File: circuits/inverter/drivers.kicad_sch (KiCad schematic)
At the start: 2 parts

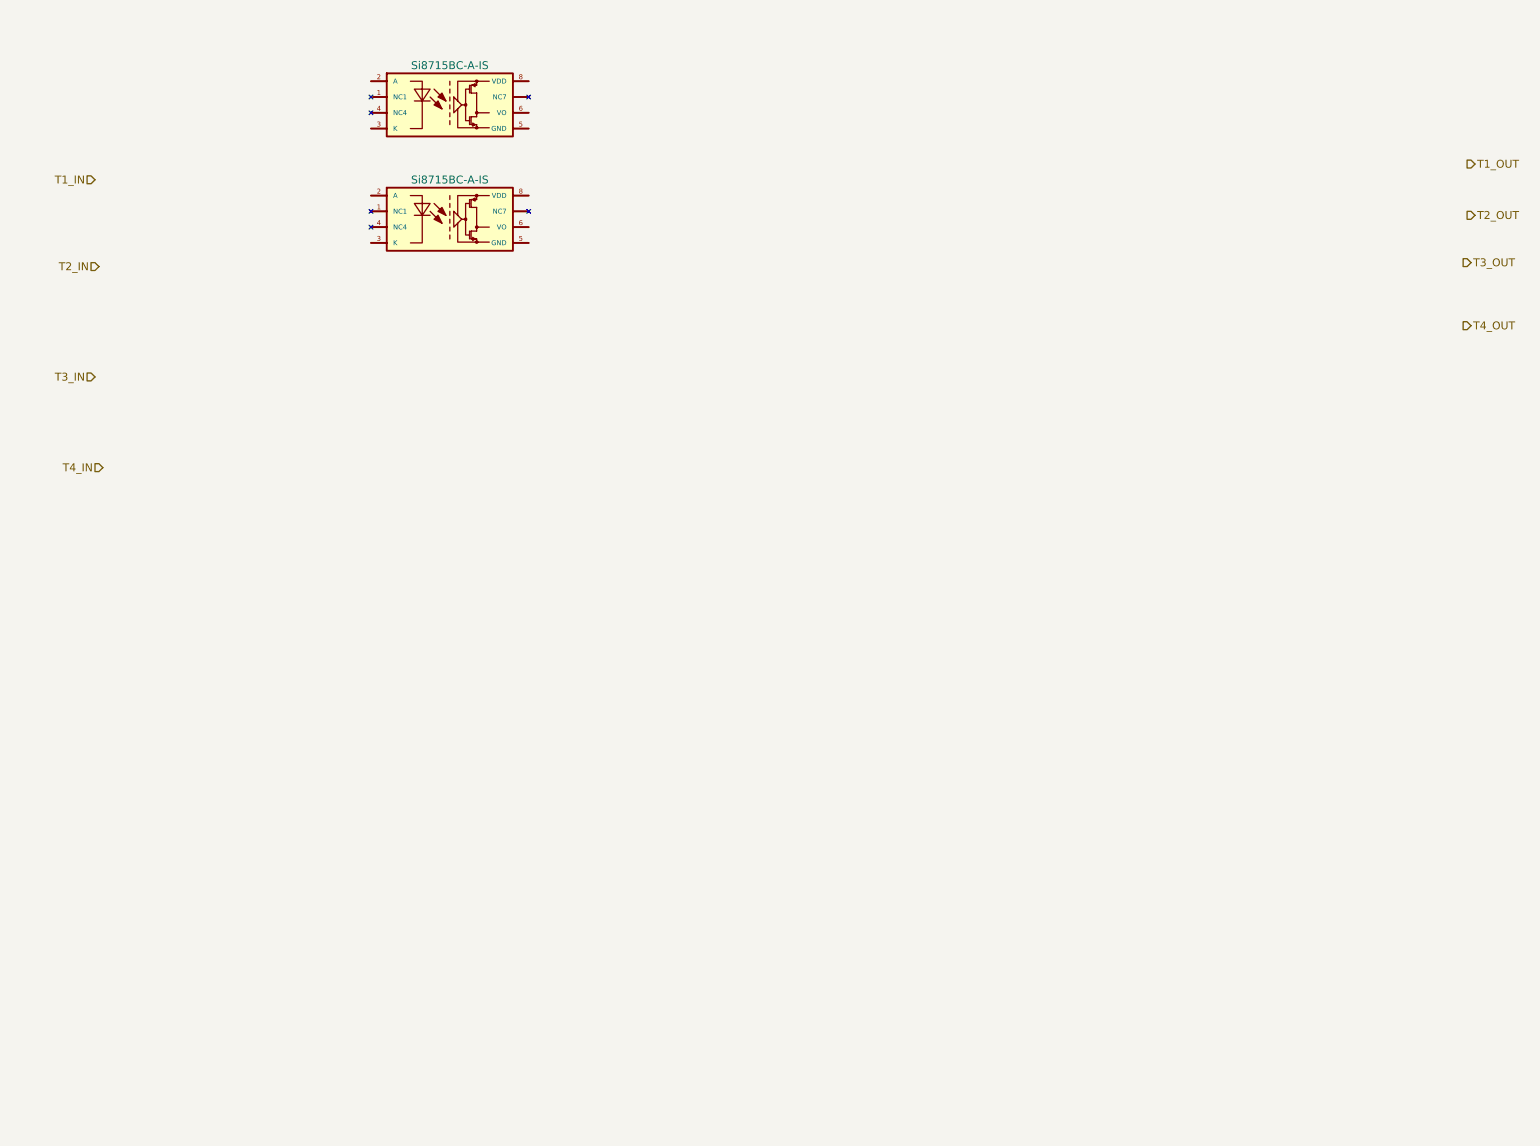
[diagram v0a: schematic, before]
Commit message: converts libraries to Kicad 6 format, updates bridge driver
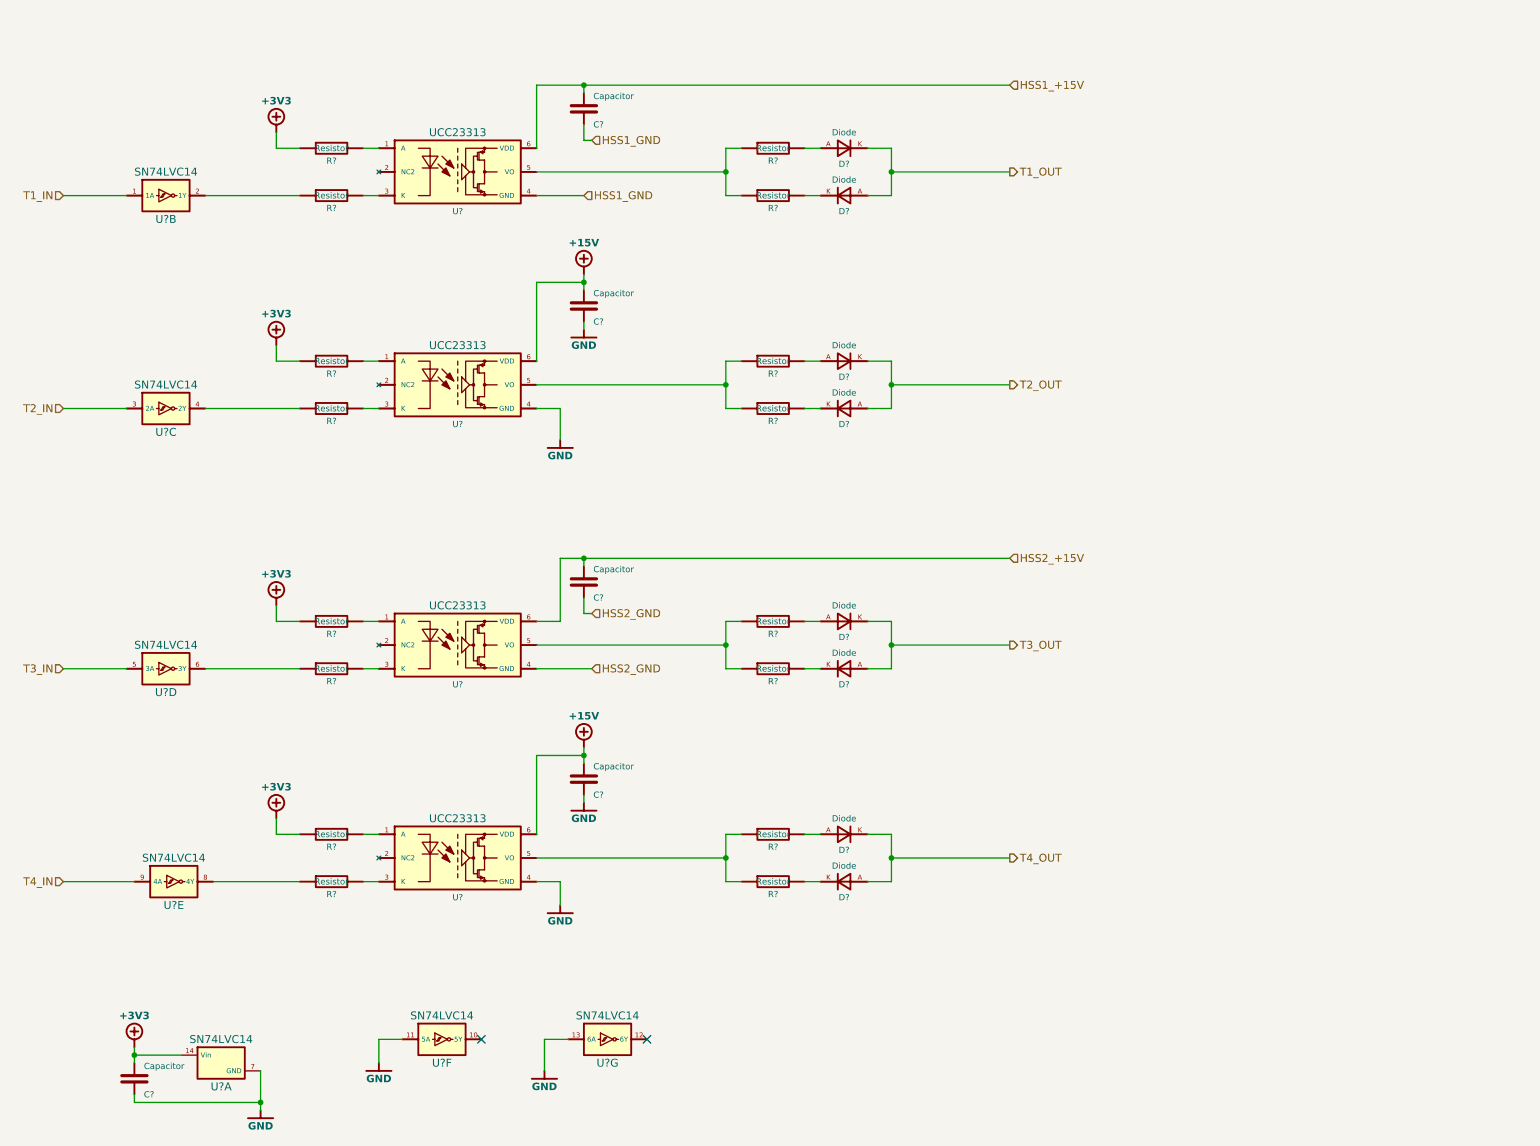
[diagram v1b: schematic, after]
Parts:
- added C? (x5): Capacitor, symbol OSSI_standard_components:Capacitor
- added D? (x8): Diode, symbol OSSI_standard_components:Diode
- added R? (x16): Resistor, symbol OSSI_standard_components:Resistor
- added U? (x7): SN74LVC14, symbol SN47HCS04:SN74LVC14
- added U? (x2): UCC23313, symbol UCC23313:UCC23313
- U? (x2): renamed from ?; value Si8715BC-A-IS -> UCC23313; symbol Si871x_2x:Si8715BC-A-IS -> UCC23313:UCC23313
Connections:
- net T1_IN: now also U?.1 (1A)
- net T1_OUT: now also D?.A, D?.K
- net T2_IN: now also U?.3 (2A)
- net T2_OUT: now also D?.A, D?.K
- net T3_IN: now also U?.5 (3A)
- net T3_OUT: now also D?.A, D?.K
- net T4_IN: now also U?.9 (4A)
- net T4_OUT: now also D?.A, D?.K
- net at U?.1 (A): now also R?.2 (x2)
- net at U?.3 (K): now also R?.2 (x2)
- net HSS1_GND: now reaches U?.4 (GND)
- net HSS1_GND: now also C?.1
- net at U?.5 (VO): now also R?.1, R?.1 (x2)
- net HSS1_+15V: now reaches U?.6 (VDD)
- net HSS1_+15V: now also C?.2
- net GND: now reaches U?.4 (GND)
- net GND: now also C?.1, C?.1, C?.1, U?.11 (5A), U?.13 (6A), U?.4 (GND), U?.7 (GND)
- net +15V: now reaches U?.6 (VDD)
- net +15V: now also C?.2, C?.2, U?.6 (VDD)
- new net: R?.1, R?.1, U?.5 (VO) (x2)
- new net: D?.K, R?.2 (x4)
- new net: R?.2, U?.1 (A) (x2)
- new net: R?.1, U?.6 (3Y)
- new net: R?.1, U?.4 (2Y)
- new net: D?.A, R?.2 (x4)
- new net: R?.1, U?.8 (4Y)
- new net: R?.2, U?.3 (K) (x2)
- new net: R?.1, U?.2 (1Y)
- new net +3V3: C?.2, R?.1, R?.1, R?.1, R?.1, U?.14 (Vin)
- new net HSS2_+15V: C?.2, U?.6 (VDD)
- new net HSS2_GND: C?.1, U?.4 (GND)
- no-connect marks 0 -> 2

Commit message: updates circuits, adds linear regulator NCP1117
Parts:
- removed C? (x3): Capacitor, symbol OSSI_standard_components:Capacitor
- removed R? (x6): Resistor, symbol OSSI_standard_components:Resistor
- added C? (x3): 1µ/50V, symbol OSSI_standard_components:Capacitor
- added R? (x6): 45.3, symbol OSSI_standard_components:Resistor
- C?: value Capacitor -> 1µ/50V
- R? (x2): value Resistor -> 45.3
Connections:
- net +15V: now also C?.2, C?.2
- net +3V3: now also R?.1, R?.1, R?.1
- net GND: now also C?.1, C?.1
- net HSS2_+15V: now also C?.2
- net HSS2_GND: now also C?.1
- net at U?.1 (A): now also R?.2 (x3)
- net at U?.3 (K): now also R?.2 (x3)
- net at U?.6 (3Y): now also R?.1
- net at U?.4 (2Y): now also R?.1
- net at U?.8 (4Y): now also R?.1
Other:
- note added: "UCC23313: V_fwd_max: 2.4 V; I_fwd: 10 mA R=(3.3 V − 2.4 V)÷10 mA = 0.9 V ÷ 10 mA = 90 Ω P=I²×R=(10 mA)²×90 Ω = 9 mW → 0603 provides enough reserve"
- note added: "uController cannot drive the LEDs directly. Inverter/Drivers required. 74xx14 can supply up to 25 mA"
